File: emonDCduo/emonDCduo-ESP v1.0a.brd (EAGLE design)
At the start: 99.1 x 76.5 mm, 85 parts, among them Q1 16Mhz XT49M-2016M, U1_TQFP ATMEGA328P

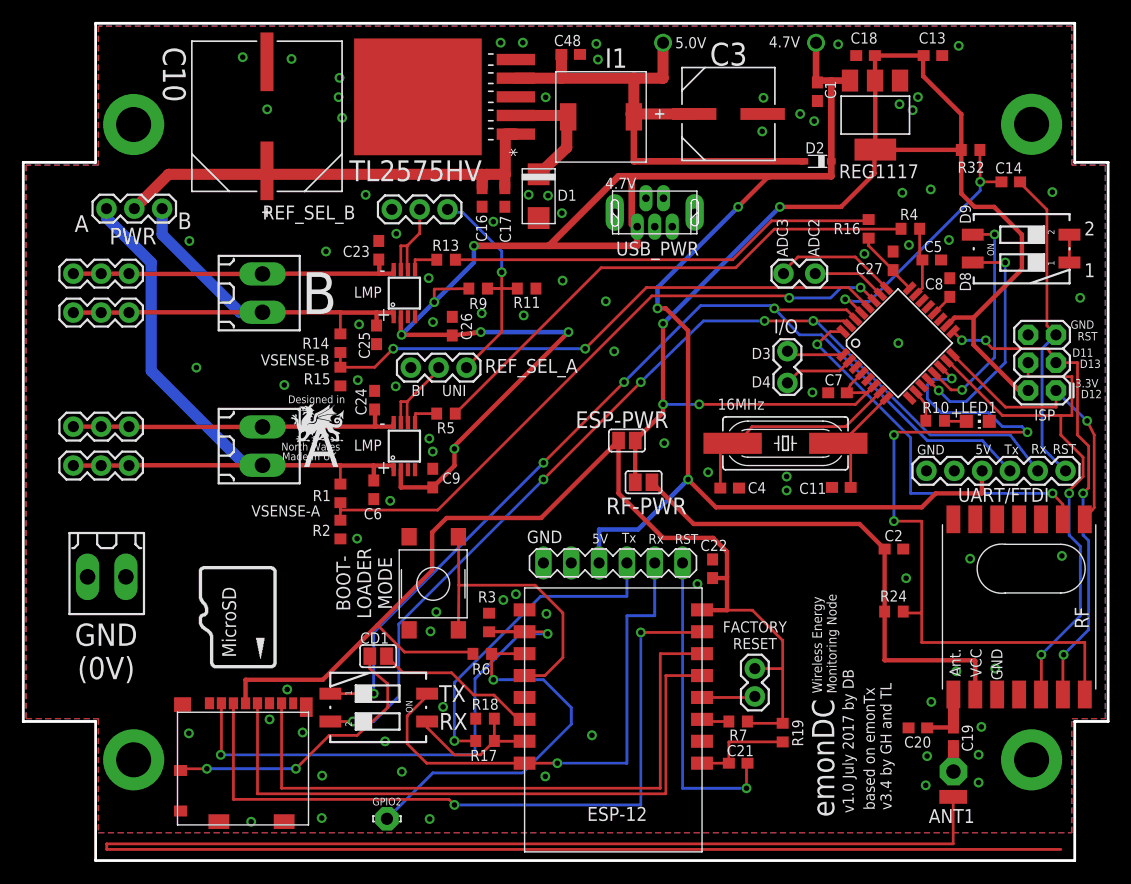
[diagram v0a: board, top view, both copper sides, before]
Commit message: new boards and library files
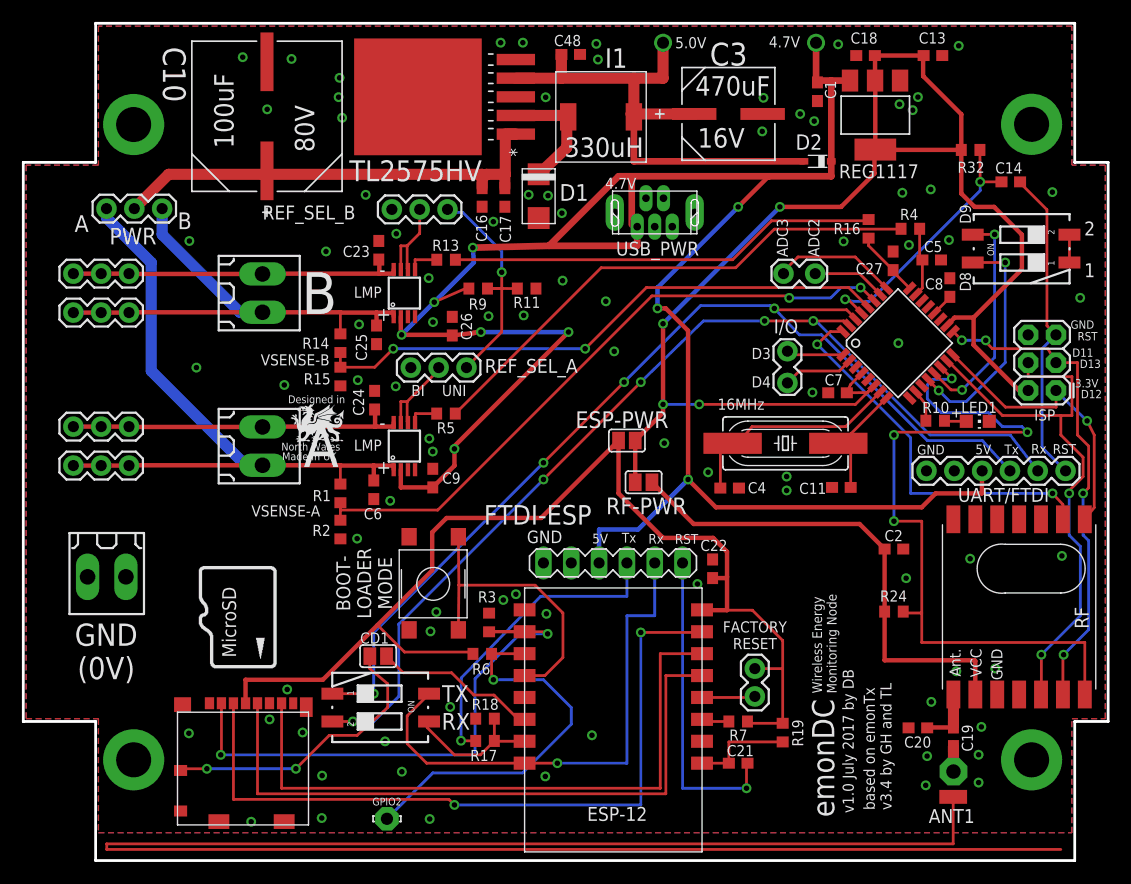
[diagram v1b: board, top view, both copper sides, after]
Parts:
- moved S1 0.18 mm to (32.7, 15.7)
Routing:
- net 4.7V: track 199.1 -> 198.1 mm
- net N$36: track 29.3 -> 28.4 mm
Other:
- board text added: "100uF"
- board text added: "16V"
- board text added: "470uF"
- board text added: "80V"
